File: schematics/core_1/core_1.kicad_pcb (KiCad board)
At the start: 2 copper layers, 100 x 91.1 mm, 22 parts, among them U1 74LS00, U2 74LS04, U3 74LS109, U4 74LS02

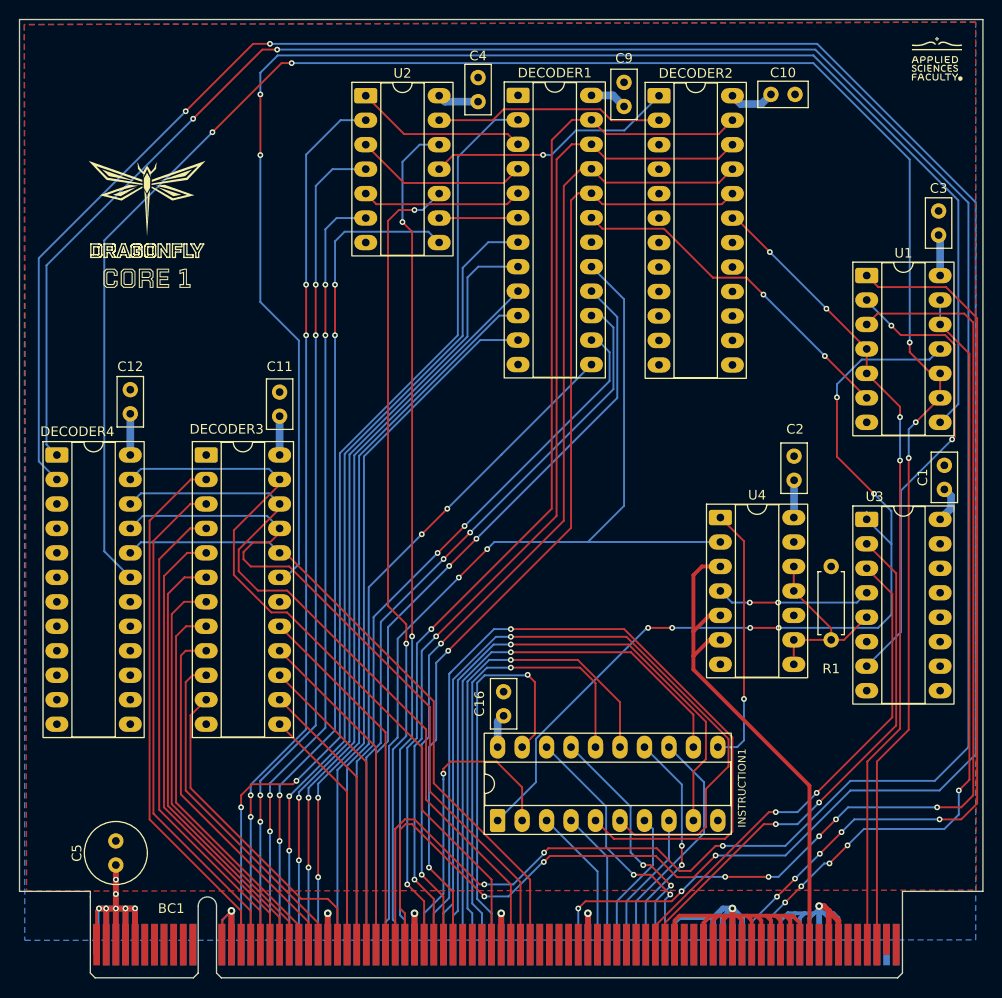
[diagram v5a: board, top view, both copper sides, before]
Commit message: Add test points
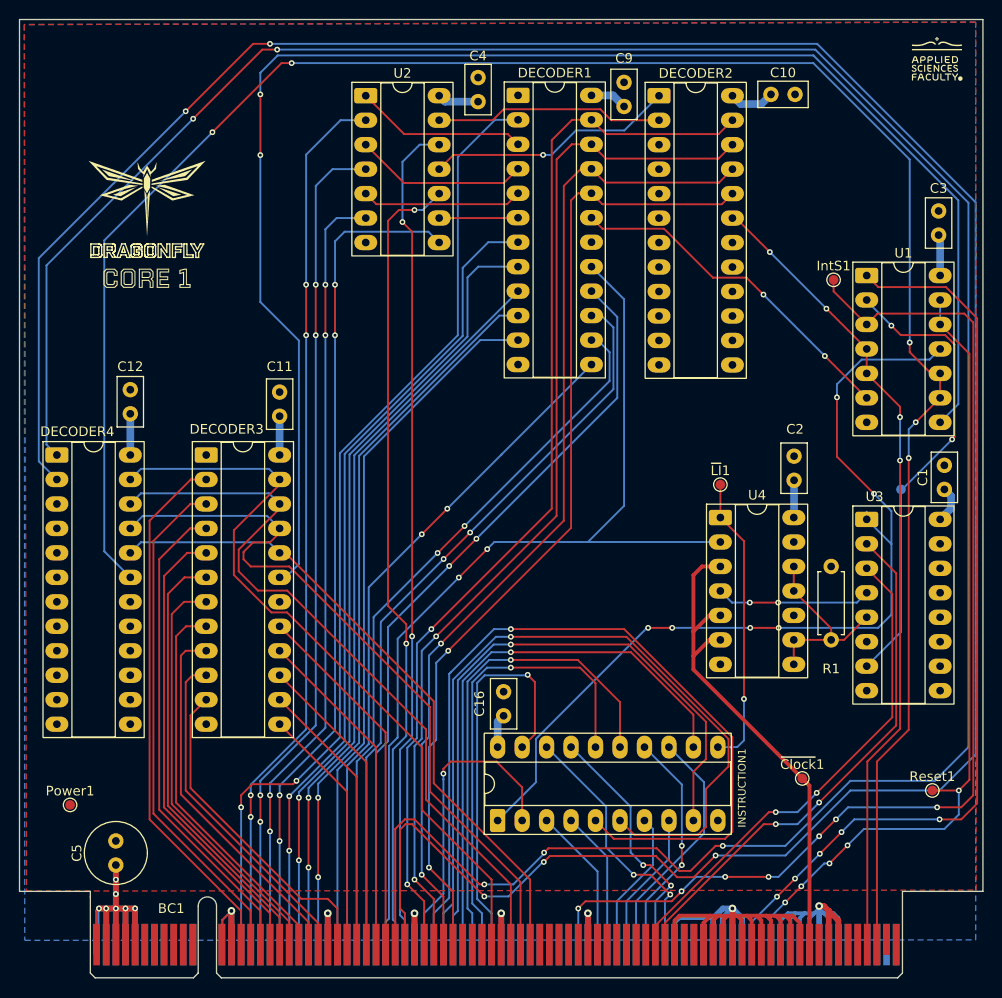
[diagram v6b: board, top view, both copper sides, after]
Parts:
- added IntS1: IntS, TestPoint:TestPoint_Pad_D1.0mm, F.Cu at (179.5, 57.5)
- added Power1: Power, TestPoint:TestPoint_Pad_D1.0mm, F.Cu at (100.2, 112.0)
- added Reset1: Reset, TestPoint:TestPoint_Pad_D1.0mm, F.Cu at (189.8, 110.5)
- added ~{Clock}1: ~{Clock}, TestPoint:TestPoint_Pad_D1.0mm, F.Cu at (176.2, 109.2)
- added ~{IntE}1: ~{IntE}, TestPoint:TestPoint_Pad_D1.0mm, B.Cu at (186.5, 79.2)
- added ~{LI}1: ~{LoadInstruction}, TestPoint:TestPoint_Pad_D1.0mm, F.Cu at (167.8, 78.8)
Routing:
- net Net-(BC1-STATE15): track 110.6 -> 116.7 mm
- net Net-(INSTRUCTION1-Cp): track 27.1 -> 30.6 mm
- net /Reset: track 81.9 -> 84.7 mm

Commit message: final review
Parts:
- ~{IntE}1: moved to F.Cu
- moved ~{IntE}1 23.3 mm to (178.2, 57.5), turned to 0 degrees
- moved IntS1 3.72 mm to (178.2, 61.0)
- moved C1 0.25 mm to (191.2, 79.2)
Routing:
- net Net-(U3A-~{Q}): track 48.3 -> 54.0 mm
- net Net-(BC1-STATE15): track 116.7 -> 115.8 mm

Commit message: done
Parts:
- added kibuzzard-691DE05D: G***, kibuzzard-691DE05D, F.Cu at (186.5, 33.0)
- added kibuzzard-691DE084: G***, kibuzzard-691DE084, F.Cu at (118.5, 65.5)
